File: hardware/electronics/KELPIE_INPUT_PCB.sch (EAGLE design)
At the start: 27 parts, among them J1 30_PIN_CONNECTOR_MALEFLEX_CON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

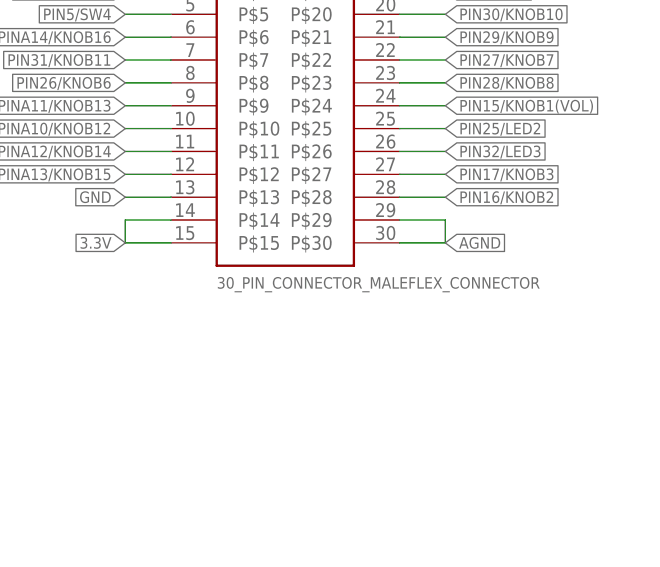
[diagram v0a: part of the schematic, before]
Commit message: board rev 2 done, sent to seeed for manufacture
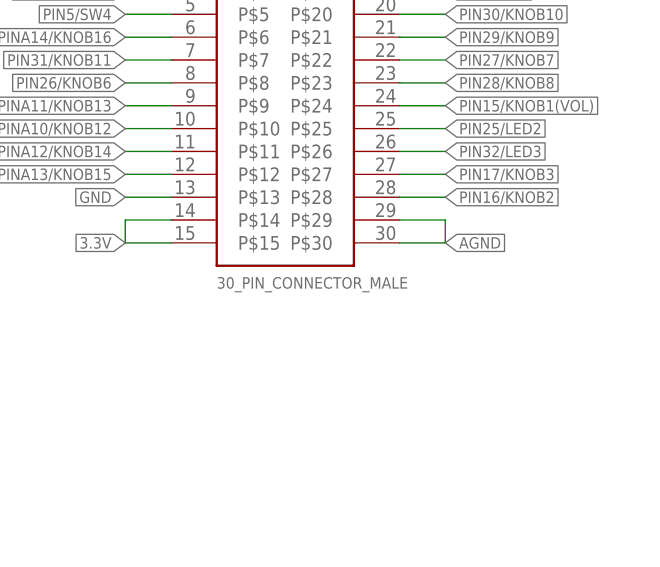
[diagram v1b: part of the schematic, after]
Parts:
- J1: value 30_PIN_CONNECTOR_MALEFLEX_CONNECTOR -> 30_PIN_CONNECTOR_MALE; device sirin-clone-library:30_PIN_CONNECTOR_MALEFLEX_CONNECTOR -> sirin-clone-library:30_PIN_CONNECTOR_MALE
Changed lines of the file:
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@@
 <?xml version="1.0" encoding="utf-8"?>
 <!DOCTYPE eagle SYSTEM "eagle.dtd">
-<eagle version="9.4.2">
+<eagle version="9.3.1">
 <drawing>
 <settings>
@@
 <part name="U$16" library="sirin-clone-library" library_urn="urn:adsk.eagle:library:9336050" deviceset="BOURNS_10K_POTENTIOMETER" device="" package3d_urn="urn:adsk.eagle:package:9336105/4"/>
 <part name="U$17" library="sirin-clone-library" library_urn="urn:adsk.eagle:library:9336050" deviceset="BOURNS_10K_POTENTIOMETER" device="" package3d_urn="urn:adsk.eagle:package:9336105/4"/>
-<part name="U$18" library="sirin-clone-library" library_urn="urn:adsk.eagle:library:9336050" deviceset="ESWITCH__YELLOW" device="" package3d_urn="urn:adsk.eagle:package:9336176/2"/>
-<part name="U$19" library="sirin-clone-library" library_urn="urn:adsk.eagle:library:9336050" deviceset="ESWITCH__YELLOW" device="" package3d_urn="urn:adsk.eagle:package:9336176/2"/>
-<part name="U$20" library="sirin-clone-library" library_urn="urn:adsk.eagle:library:9336050" deviceset="ESWITCH__YELLOW" device="" package3d_urn="urn:adsk.eagle:package:9336176/2"/>
-<part name="U$21" library="sirin-clone-library" library_urn="urn:adsk.eagle:library:9336050" deviceset="ESWITCH__YELLOW" device="" package3d_urn="urn:adsk.eagle:package:9336176/2"/>
-<part name="J1" library="sirin-clone-library" library_urn="urn:adsk.eagle:library:9336050" deviceset="30_PIN_CONNECTOR_MALE" device="FLEX_CONNECTOR" package3d_urn="urn:adsk.eagle:package:12919137/6" value="30_PIN_CONNECTOR_MALEFLEX_CONNECTOR">
+<part name="U$18" library="sirin-clone-library" library_urn="urn:adsk.eagle:library:9336050" deviceset="ESWITCH__YELLOW" device="" package3d_urn="urn:adsk.eagle:package:9336176/3"/>
+<part name="U$19" library="sirin-clone-library" library_urn="urn:adsk.eagle:library:9336050" deviceset="ESWITCH__YELLOW" device="" package3d_urn="urn:adsk.eagle:package:9336176/3"/>
+<part name="U$20" library="sirin-clone-library" library_urn="urn:adsk.eagle:library:9336050" deviceset="ESWITCH__YELLOW" device="" package3d_urn="urn:adsk.eagle:package:9336176/3"/>
+<part name="U$21" library="sirin-clone-library" library_urn="urn:adsk.eagle:library:9336050" deviceset="ESWITCH__YELLOW" device="" package3d_urn="urn:adsk.eagle:package:9336176/3"/>
+<part name="J1" library="sirin-clone-library" library_urn="urn:adsk.eagle:library:9336050" deviceset="30_PIN_CONNECTOR_MALE" device="" package3d_urn="urn:adsk.eagle:package:12956103/2" value="30_PIN_CONNECTOR_MALE">
 <attribute name="SPICEPREFIX" value="X"/>
 </part>
